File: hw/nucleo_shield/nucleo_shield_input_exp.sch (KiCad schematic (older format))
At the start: 3 parts, among them U14 PCF8574A, U7 PCF8574A, U8 PCF8574A

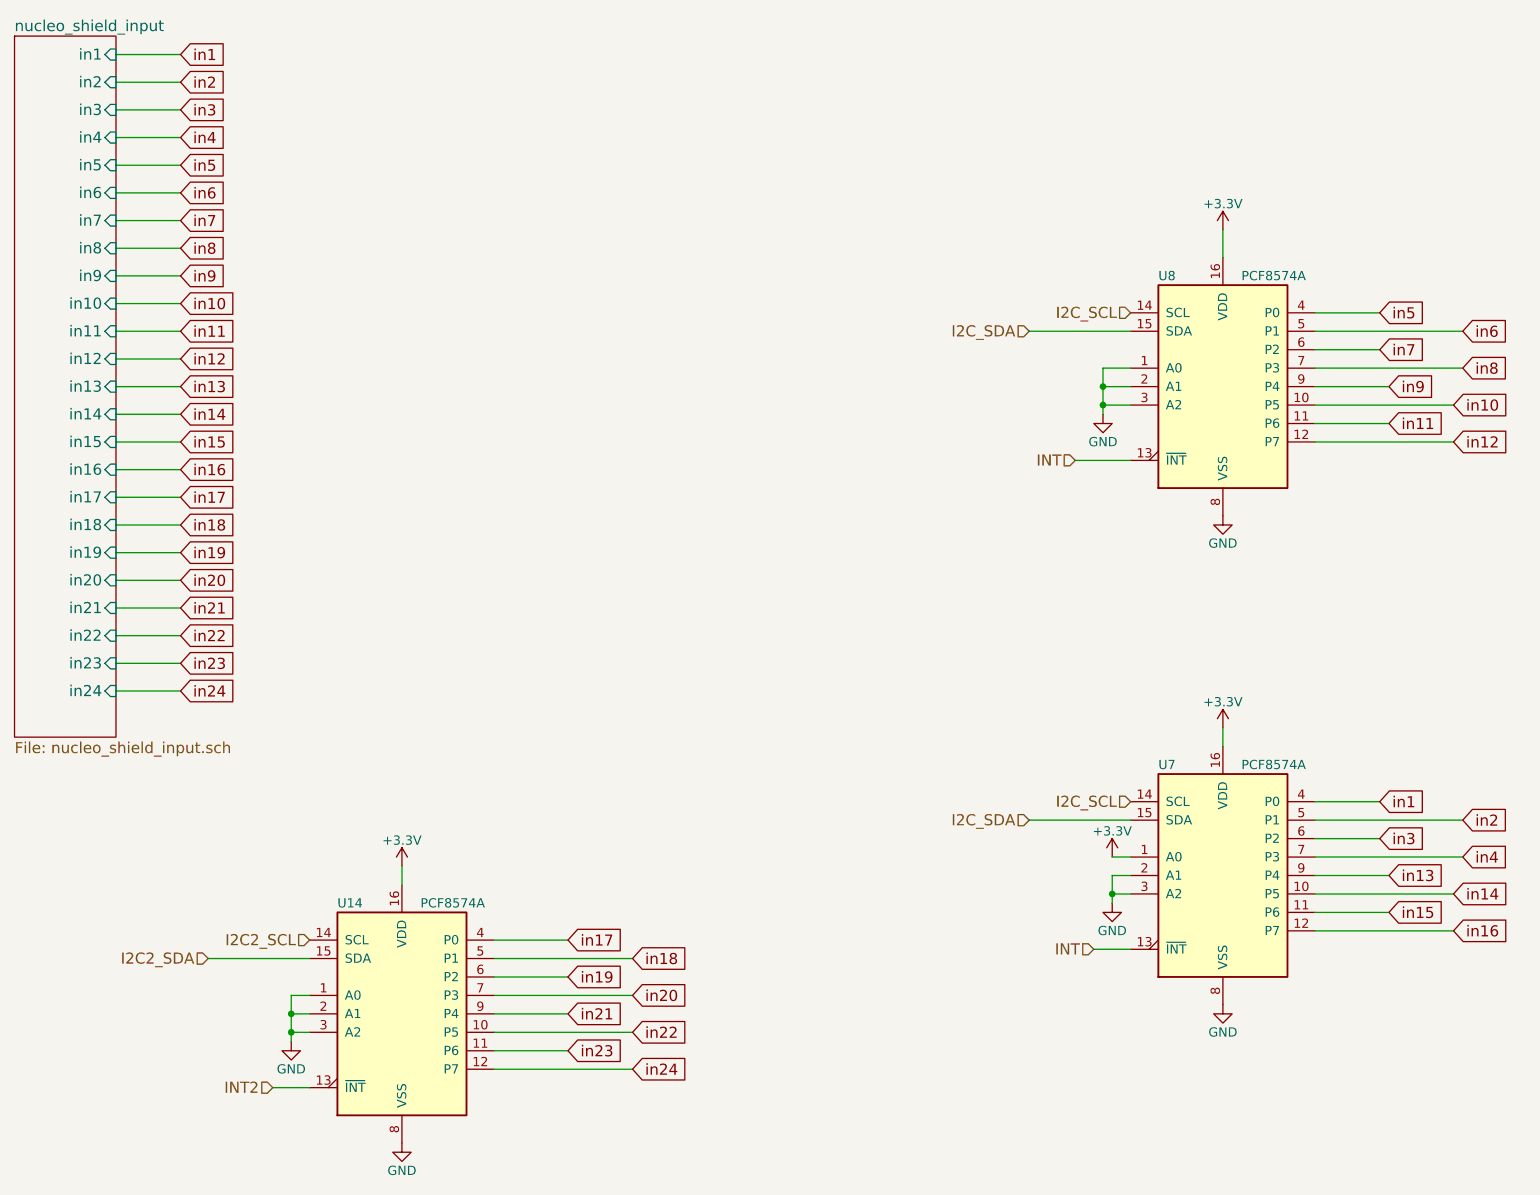
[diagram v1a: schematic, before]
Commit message: Nucleo: Remove input pullup on pcf
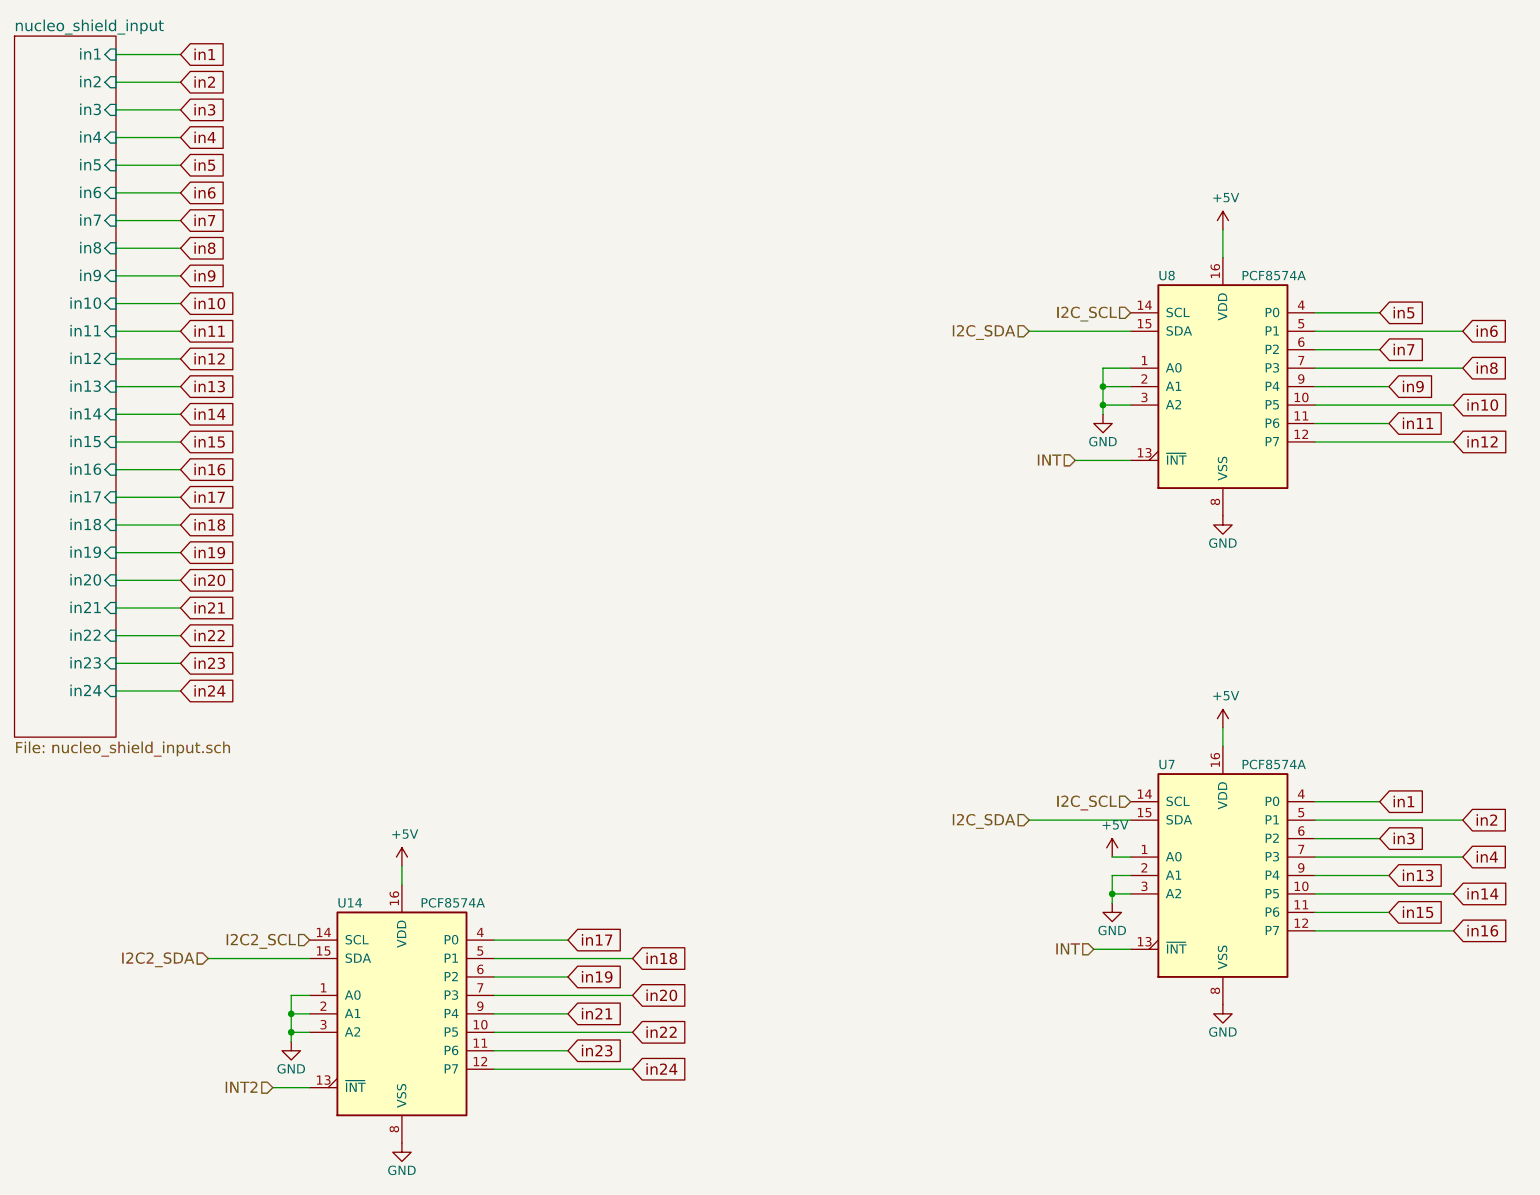
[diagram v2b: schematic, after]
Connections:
- net +3V3 renamed +5V
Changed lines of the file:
@@
 $EndComp
 $Comp
-L +3.3V #PWR38
-U 1 1 572B2AC4
-P 9400 1950
-F 0 "#PWR38" H 9400 1800 50  0001 C CNN
-F 1 "+3.3V" H 9400 2090 50  0000 C CNN
-F 2 "" H 9400 1950 60  0000 C CNN
-F 3 "" H 9400 1950 60  0000 C CNN
-	1    9400 1950
-	1    0    0    -1
-$EndComp
-$Comp
-L +3.3V #PWR40
-U 1 1 572B2ACA
-P 9400 4650
-F 0 "#PWR40" H 9400 4500 50  0001 C CNN
-F 1 "+3.3V" H 9400 4790 50  0000 C CNN
-F 2 "" H 9400 4650 60  0000 C CNN
-F 3 "" H 9400 4650 60  0000 C CNN
-	1    9400 4650
-	1    0    0    -1
-$EndComp
-$Comp
-L GND #PWR39
+L GND #PWR034
 U 1 1 572B2AD2
 P 9400 3500
-F 0 "#PWR39" H 9400 3250 50  0001 C CNN
+F 0 "#PWR034" H 9400 3250 50  0001 C CNN
 F 1 "GND" H 9400 3350 50  0000 C CNN
 F 2 "" H 9400 3500 60  0000 C CNN
@@
 $EndComp
 $Comp
-L GND #PWR41
+L GND #PWR035
 U 1 1 572B2AD8
 P 9400 6150
-F 0 "#PWR41" H 9400 5900 50  0001 C CNN
+F 0 "#PWR035" H 9400 5900 50  0001 C CNN
 F 1 "GND" H 9400 6000 50  0000 C CNN
 F 2 "" H 9400 6150 60  0000 C CNN
@@
 INT
 $Comp
-L GND #PWR35
+L GND #PWR036
 U 1 1 572AA068
 P 8750 2950
-F 0 "#PWR35" H 8750 2700 50  0001 C CNN
+F 0 "#PWR036" H 8750 2700 50  0001 C CNN
 F 1 "GND" H 8750 2800 50  0000 C CNN
 F 2 "" H 8750 2950 60  0000 C CNN
@@
 $EndComp
 $Comp
-L GND #PWR37
+L GND #PWR037
 U 1 1 572AAB50
 P 8800 5600
-F 0 "#PWR37" H 8800 5350 50  0001 C CNN
+F 0 "#PWR037" H 8800 5350 50  0001 C CNN
 F 1 "GND" H 8800 5450 50  0000 C CNN
 F 2 "" H 8800 5600 60  0000 C CNN
 F 3 "" H 8800 5600 60  0000 C CNN
 	1    8800 5600
-	1    0    0    -1
-$EndComp
-$Comp
-L +3.3V #PWR36
-U 1 1 572AAEDA
-P 8800 5350
-F 0 "#PWR36" H 8800 5200 50  0001 C CNN
-F 1 "+3.3V" H 8800 5490 50  0000 C CNN
-F 2 "" H 8800 5350 60  0000 C CNN
-F 3 "" H 8800 5350 60  0000 C CNN
-	1    8800 5350
 	1    0    0    -1
 $EndComp
@@
 $EndComp
 $Comp
-L +3.3V #PWR33
-U 1 1 5767DB4C
-P 4950 5400
-F 0 "#PWR33" H 4950 5250 50  0001 C CNN
-F 1 "+3.3V" H 4950 5540 50  0000 C CNN
-F 2 "" H 4950 5400 60  0000 C CNN
-F 3 "" H 4950 5400 60  0000 C CNN
-	1    4950 5400
-	1    0    0    -1
-$EndComp
-$Comp
-L GND #PWR34
+L GND #PWR040
 U 1 1 5767DB53
 P 4950 6900
-F 0 "#PWR34" H 4950 6650 50  0001 C CNN
+F 0 "#PWR040" H 4950 6650 50  0001 C CNN
 F 1 "GND" H 4950 6750 50  0000 C CNN
 F 2 "" H 4950 6900 60  0000 C CNN
@@
 INT2
 $Comp
-L GND #PWR32
+L GND #PWR041
 U 1 1 5767DB61
 P 4350 6350
-F 0 "#PWR32" H 4350 6100 50  0001 C CNN
+F 0 "#PWR041" H 4350 6100 50  0001 C CNN
 F 1 "GND" H 4350 6200 50  0000 C CNN
 F 2 "" H 4350 6350 60  0000 C CNN
@@
 	4450 6100 4350 6100
 Connection ~ 4350 6200
+$Comp
+L +5V #PWR?
+U 1 1 5785C417
+P 4950 5400
+F 0 "#PWR?" H 4950 5250 50  0001 C CNN
+F 1 "+5V" H 4965 5573 50  0000 C CNN
+F 2 "" H 4950 5400 50  0000 C CNN
+F 3 "" H 4950 5400 50  0000 C CNN
+	1    4950 5400
+	1    0    0    -1
+$EndComp
+$Comp
+L +5V #PWR?
+U 1 1 5785C4C2
+P 9400 4650
+F 0 "#PWR?" H 9400 4500 50  0001 C CNN
+F 1 "+5V" H 9415 4823 50  0000 C CNN
+F 2 "" H 9400 4650 50  0000 C CNN
+F 3 "" H 9400 4650 50  0000 C CNN
+	1    9400 4650
+	1    0    0    -1
+$EndComp
+$Comp
+L +5V #PWR?
+U 1 1 5785C566
+P 9400 1950
+F 0 "#PWR?" H 9400 1800 50  0001 C CNN
+F 1 "+5V" H 9415 2123 50  0000 C CNN
+F 2 "" H 9400 1950 50  0000 C CNN
+F 3 "" H 9400 1950 50  0000 C CNN
+	1    9400 1950
+	1    0    0    -1
+$EndComp
+$Comp
+L +5V #PWR?
+U 1 1 5785F361
+P 8800 5350
+F 0 "#PWR?" H 8800 5200 50  0001 C CNN
+F 1 "+5V" H 8815 5523 50  0000 C CNN
+F 2 "" H 8800 5350 50  0000 C CNN
+F 3 "" H 8800 5350 50  0000 C CNN
+	1    8800 5350
+	1    0    0    -1
+$EndComp
 $EndSCHEMATC
